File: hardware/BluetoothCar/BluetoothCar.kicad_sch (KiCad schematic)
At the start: 26 parts, among them J2 Jack_DC, J3 LCD 1602, J4 Conn_01x06, J5 Servo_Motor, J6 Battery_Source, M1 Motor_DC, M2 Motor_DC, U1 ESP32-DevKitC

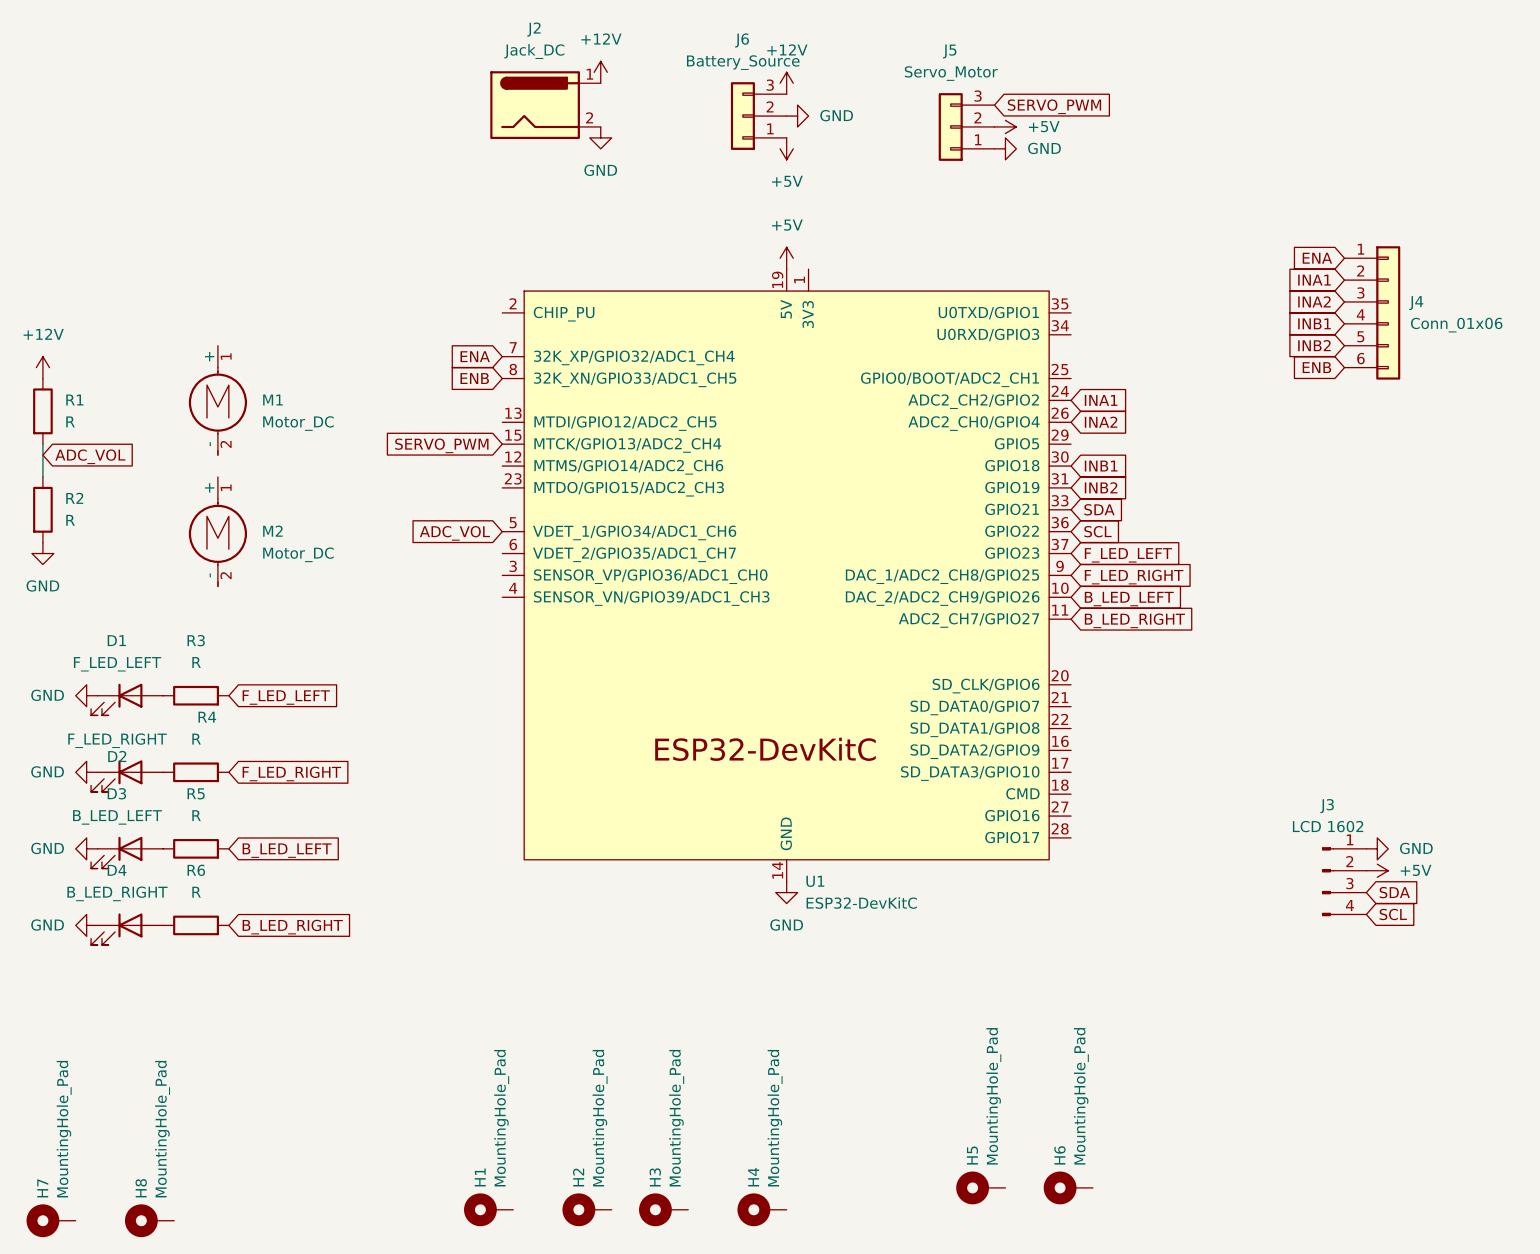
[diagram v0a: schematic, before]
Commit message: Modify ln298 channel b
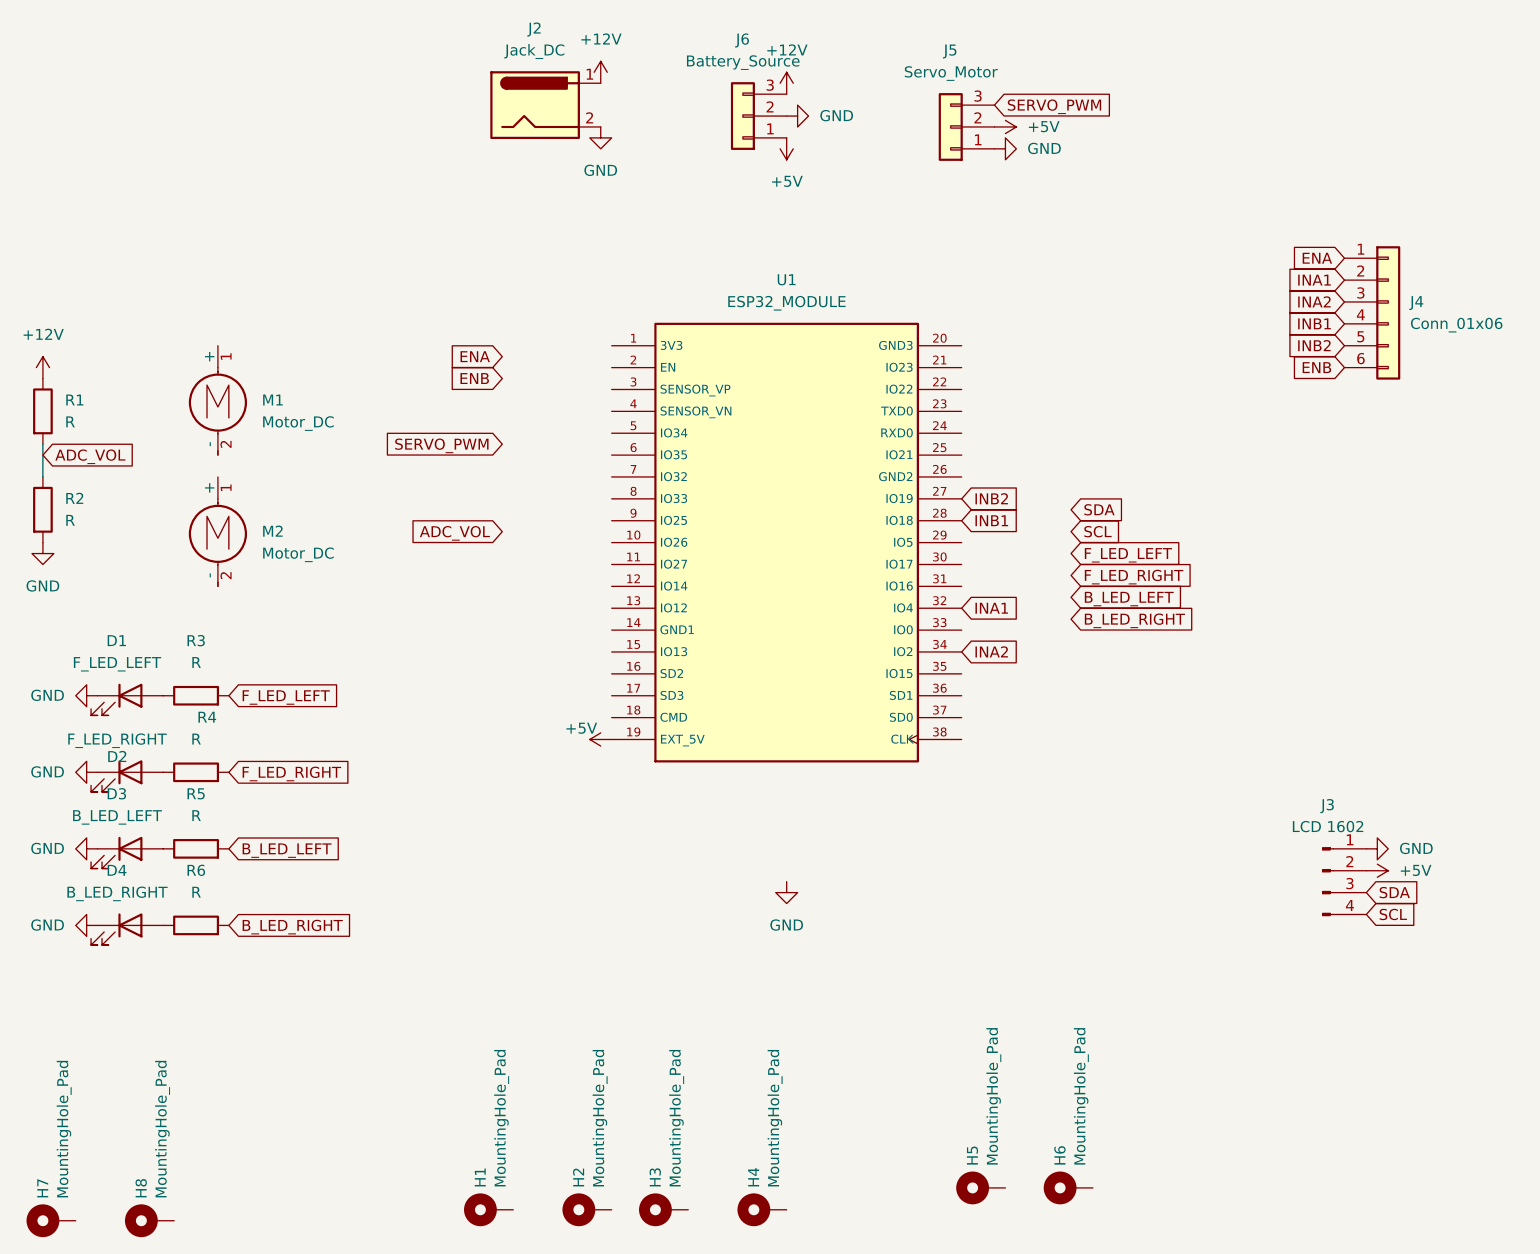
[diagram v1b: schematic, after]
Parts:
- removed U1: ESP32-DevKitC, ESP32_DAT:MODULE_ESP32-DEVKITC-32D, symbol ESP32:ESP32-DevKitC
- added U1: ESP32_MODULE, ESP32-DEVKITC-32D:MODULE_ESP32-DEVKITC-32D-Big-hole, symbol Main_PCB:ESP32_MODULE
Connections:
- net +5V: now also U1.19 (EXT_5V)
- net INA1: now also U1.32 (IO4)
- net INA2: now also U1.34 (IO2)
- net INB1: now also U1.28 (IO18)
- net INB2: now also U1.27 (IO19)
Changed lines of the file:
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@@
 	(global_label "INB1"
 		(shape input)
-		(at 154.94 80.01 0)
+		(at 142.24 86.36 0)
 		(fields_autoplaced yes)
 		(effects
@@
 		)
 		(property "Intersheetrefs" "${INTERSHEET_REFS}"
-			(at 162.34 80.01 0)
+			(at 149.64 86.36 0)
 			(effects
 				(font
@@
 	(global_label "INB2"
 		(shape input)
-		(at 154.94 82.55 0)
+		(at 142.24 83.82 0)
 		(fields_autoplaced yes)
 		(effects
@@
 		)
 		(property "Intersheetrefs" "${INTERSHEET_REFS}"
-			(at 162.34 82.55 0)
+			(at 149.64 83.82 0)
 			(effects
 				(font
@@
 	(global_label "INA1"
 		(shape input)
-		(at 154.94 72.39 0)
+		(at 142.24 96.52 0)
 		(fields_autoplaced yes)
 		(effects
@@
 		)
 		(property "Intersheetrefs" "${INTERSHEET_REFS}"
-			(at 162.1586 72.39 0)
+			(at 149.4586 96.52 0)
 			(effects
 				(font
@@
 	(global_label "INA2"
 		(shape input)
-		(at 154.94 74.93 0)
+		(at 142.24 101.6 0)
 		(fields_autoplaced yes)
 		(effects
@@
 		)
 		(property "Intersheetrefs" "${INTERSHEET_REFS}"
-			(at 162.1586 74.93 0)
+			(at 149.4586 101.6 0)
 			(effects
 				(font
@@
 	)
 	(symbol
+		(lib_id "Main_PCB:ESP32_MODULE")
+		(at 121.92 88.9 0)
+		(unit 1)
+		(exclude_from_sim no)
+		(in_bom no)
+		(on_board yes)
+		(dnp no)
+		(fields_autoplaced yes)
+		(property "Reference" "U1"
+			(at 121.92 58.42 0)
+			(effects
+				(font
+					(size 1.27 1.27)
+				)
+			)
+		)
+		(property "Value" "ESP32_MODULE"
+			(at 121.92 60.96 0)
+			(effects
+				(font
+					(size 1.27 1.27)
+				)
+			)
+		)
+		(property "Footprint" "ESP32-DEVKITC-32D:MODULE_ESP32-DEVKITC-32D-Big-hole"
+			(at 118.11 88.9 0)
+			(effects
+				(font
+					(size 1.27 1.27)
+				)
+				(hide yes)
+			)
+		)
+		(property "Datasheet" ""
+			(at 118.11 88.9 0)
+			(effects
+				(font
+					(size 1.27 1.27)
+				)
+				(hide yes)
+			)
+		)
+		(property "Description" ""
+			(at 121.92 88.9 0)
+			(effects
+				(font
+					(size 1.27 1.27)
+				)
+			)
+		)
+		(pin "1"
+		)
+		(pin "10"
+		)
+		(pin "11"
+		)
+		(pin "12"
+		)
+		(pin "13"
+		)
+		(pin "14"
+		)
+		(pin "15"
+		)
+		(pin "16"
+		)
+		(pin "17"
+		)
+		(pin "18"
+		)
+		(pin "19"
+		)
+		(pin "2"
+		)
+		(pin "20"
+		)
+		(pin "21"
+		)
+		(pin "22"
+		)
+		(pin "23"
+		)
+		(pin "24"
+		)
+		(pin "25"
+		)
+		(pin "26"
+		)
+		(pin "27"
+		)
+		(pin "28"
+		)
+		(pin "29"
+		)
+		(pin "3"
+		)
+		(pin "30"
+		)
+		(pin "31"
+		)
+		(pin "32"
+		)
+		(pin "33"
+		)
+		(pin "34"
+		)
+		(pin "35"
+		)
+		(pin "36"
+		)
+		(pin "37"
+		)
+		(pin "38"
+		)
+		(pin "4"
+		)
+		(pin "5"
+		)
+		(pin "6"
+		)
+		(pin "7"
+		)
+		(pin "8"
+		)
+		(pin "9"
+		)
+		(instances
+			(project "BluetoothCar"
+				(path "/1cad5022-0245-4951-ae01-deeddb943356"
+					(reference "U1")
+					(unit 1)
+				)
+			)
+		)
+	)
+	(symbol
 		(lib_id "Device:LED")
 		(at 45.72 106.68 0)
@@
 	(symbol
 		(lib_id "power:+5V")
-		(at 121.92 57.15 0)
+		(at 101.6 111.76 90)
 		(unit 1)
 		(exclude_from_sim no)
@@
 		(on_board yes)
 		(dnp no)
-		(fields_autoplaced yes)
 		(property "Reference" "#PWR06"
-			(at 121.92 60.96 0)
+			(at 105.41 111.76 0)
 			(effects
 				(font
@@
 		)
 		(property "Value" "+5V"
-			(at 121.92 52.07 0)
+			(at 98.044 110.49 90)
 			(effects
 				(font
@@
 		)
 		(property "Footprint" ""
-			(at 121.92 57.15 0)
+			(at 101.6 111.76 0)
 			(effects
 				(font
@@
 		)
 		(property "Datasheet" ""
-			(at 121.92 57.15 0)
+			(at 101.6 111.76 0)
 			(effects
 				(font
@@
 		)
 		(property "Description" "Power symbol creates a global label with name \"+5V\""
-			(at 121.92 57.15 0)
+			(at 101.6 111.76 0)
 			(effects
 				(font
@@
 					(unit 1)
 				)
-			)
-		)
-	)
-	(symbol
-		(lib_id "ESP32:ESP32-DevKitC")
-		(at 121.92 92.71 0)
-		(unit 1)
-		(exclude_from_sim no)
-		(in_bom yes)
-		(on_board yes)
-		(dnp no)
-		(fields_autoplaced yes)
-		(property "Reference" "U1"
-			(at 124.0633 128.27 0)
-			(effects
-				(font
-					(size 1.27 1.27)
-				)
-				(justify left)
-			)
-		)
-		(property "Value" "ESP32-DevKitC"
-			(at 124.0633 130.81 0)
-			(effects
-				(font
-					(size 1.27 1.27)
-				)
-				(justify left)
-			)
-		)
-		(property "Footprint" "ESP32_DAT:MODULE_ESP32-DEVKITC-32D"
-			(at 121.92 135.89 0)
-			(effects
-				(font
-					(size 1.27 1.27)
-				)
-				(hide yes)
-			)
-		)
-		(property "Datasheet" "https://docs.espressif.com/projects/esp-idf/zh_CN/latest/esp32/hw-reference/esp32/get-started-devkitc.html"
-			(at 121.92 138.43 0)
-			(effects
-				(font
-					(size 1.27 1.27)
-				)
-				(hide yes)
-			)
-		)
-		(property "Description" "Development Kit"
-			(at 121.92 92.71 0)
-			(effects
-				(font
-					(size 1.27 1.27)
-				)
-				(hide yes)
-			)
-		)
-		(pin "1"
-		)
-		(pin "23"
-		)
-		(pin "28"
-		)
-		(pin "20"
-		)
-		(pin "21"
-		)
-		(pin "36"
-		)
-		(pin "22"
-		)
-		(pin "27"
-		)
-		(pin "2"
-		)
-		(pin "12"
-		)
-		(pin "17"
-		)
-		(pin "26"
-		)
-		(pin "38"
-		)
-		(pin "30"
-		)
-		(pin "32"
-		)
-		(pin "4"
-		)
-		(pin "29"
-		)
-		(pin "13"
-		)
-		(pin "8"
-		)
-		(pin "24"
-		)
-		(pin "15"
-		)
-		(pin "6"
-		)
-		(pin "3"
-		)
-		(pin "5"
-		)
-		(pin "31"
-		)
-		(pin "34"
-		)
-		(pin "11"
-		)
-		(pin "25"
-		)
-		(pin "35"
-		)
-		(pin "10"
-		)
-		(pin "14"
-		)
-		(pin "19"
-		)
-		(pin "16"
-		)
-		(pin "37"
-		)
-		(pin "7"
-		)
-		(pin "9"
-		)
-		(pin "33"
-		)
-		(pin "18"
-		)
-		(instances
-			(project ""
-				(path "/1cad5022-0245-4951-ae01-deeddb943356"
-					(reference "U1")
-					(unit 1)
-				)
